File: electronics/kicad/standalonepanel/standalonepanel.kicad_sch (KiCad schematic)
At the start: 84 parts, among them J1 Speaker, J2 POWER, P1 USB-C, P2 USB-A, SW1 TST-ESP32, SW2 BOOT, SW3 TST-ICE40, SW4 RESET, U1 SC189ZSKTRT, U10 MPU-6050, U2 SC189ZSKTRT, U3 ESP32-WROVER-E, U4 CH340C, U5 MAX3421E, U6 IS64WV25616EFBLL-10TLI, U7 ICE40-HX4K, U8 DS3231M, U9 MAX98357A, X2 12MHz

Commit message: fix schematic errors: - swapped TxD/RxD + resistor CH340 - corrected footprint of DS3231 (was too big) textual errors of U2 (C-variant 1.2V)
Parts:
- D2: value 1N5819WS -> BAT760
- R2: value 33R -> 47R
- U2: value SC189ZSKTRT -> SC189CSKTRT
- U8: value DS3231M -> DS3231; footprint Package_SO:SO-16_3.9x9.9mm_P1.27mm -> Package_SO:SOIC-16W_7.5x10.3mm_P1.27mm
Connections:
- net at U3.34 (U0RXD/GPIO3): now also R2.1; no longer U4.3 (RXD)
- net at U3.35 (U0TXD/GPIO1): now also U4.3 (RXD); no longer R2.1
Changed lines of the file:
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@@
 	(wire
 		(pts
-			(xy 318.77 33.02) (xy 396.24 33.02)
+			(xy 318.77 33.02) (xy 374.65 33.02)
 		)
 		(stroke
@@
 	(wire
 		(pts
-			(xy 393.7 30.48) (xy 393.7 63.5)
-		)
-		(stroke
-			(width 0)
-			(type default)
-		)
-	)
-	(wire
-		(pts
 			(xy 269.24 173.99) (xy 278.13 173.99)
 		)
@@
 	(wire
 		(pts
-			(xy 383.54 30.48) (xy 393.7 30.48)
-		)
-		(stroke
-			(width 0)
-			(type default)
-		)
-	)
-	(wire
-		(pts
 			(xy 60.96 142.24) (xy 62.23 142.24)
 		)
@@
 	(wire
 		(pts
+			(xy 398.78 66.04) (xy 398.78 30.48)
+		)
+		(stroke
+			(width 0)
+			(type default)
+		)
+	)
+	(wire
+		(pts
 			(xy 318.77 55.88) (xy 320.04 55.88)
 		)
@@
 	(wire
 		(pts
-			(xy 318.77 30.48) (xy 375.92 30.48)
-		)
-		(stroke
-			(width 0)
-			(type default)
-		)
-	)
-	(wire
-		(pts
-			(xy 388.62 66.04) (xy 396.24 66.04)
+			(xy 318.77 30.48) (xy 398.78 30.48)
 		)
 		(stroke
@@
 	(wire
 		(pts
-			(xy 396.24 33.02) (xy 396.24 66.04)
-		)
-		(stroke
-			(width 0)
-			(type default)
-		)
-	)
-	(wire
-		(pts
 			(xy 60.96 106.68) (xy 62.23 106.68)
 		)
@@
 	(wire
 		(pts
+			(xy 388.62 66.04) (xy 398.78 66.04)
+		)
+		(stroke
+			(width 0)
+			(type default)
+		)
+	)
+	(wire
+		(pts
 			(xy 372.11 170.18) (xy 375.92 170.18)
 		)
@@
 	(wire
 		(pts
-			(xy 80.01 154.94) (xy 80.01 158.75)
+			(xy 396.24 33.02) (xy 396.24 63.5)
 		)
 		(stroke
@@
 	(wire
 		(pts
-			(xy 74.93 44.45) (xy 74.93 45.72)
+			(xy 80.01 154.94) (xy 80.01 158.75)
 		)
 		(stroke
@@
 	(wire
 		(pts
-			(xy 137.16 71.12) (xy 137.16 72.39)
+			(xy 74.93 44.45) (xy 74.93 45.72)
 		)
 		(stroke
@@
 	(wire
 		(pts
-			(xy 317.5 127) (xy 322.58 127)
+			(xy 137.16 71.12) (xy 137.16 72.39)
 		)
 		(stroke
@@
 	(wire
 		(pts
-			(xy 149.86 45.72) (xy 170.18 45.72)
+			(xy 317.5 127) (xy 322.58 127)
 		)
 		(stroke
@@
 	(wire
 		(pts
-			(xy 167.64 195.58) (xy 167.64 209.55)
+			(xy 149.86 45.72) (xy 170.18 45.72)
 		)
 		(stroke
@@
 	(wire
 		(pts
-			(xy 262.89 162.56) (xy 262.89 163.83)
+			(xy 167.64 195.58) (xy 167.64 209.55)
 		)
 		(stroke
@@
 	(wire
 		(pts
-			(xy 388.62 63.5) (xy 393.7 63.5)
+			(xy 262.89 162.56) (xy 262.89 163.83)
 		)
 		(stroke
@@
 	(wire
 		(pts
+			(xy 382.27 33.02) (xy 396.24 33.02)
+		)
+		(stroke
+			(width 0)
+			(type default)
+		)
+	)
+	(wire
+		(pts
 			(xy 88.9 30.48) (xy 93.98 30.48)
 		)
@@
 	(wire
 		(pts
+			(xy 396.24 63.5) (xy 388.62 63.5)
+		)
+		(stroke
+			(width 0)
+			(type default)
+		)
+	)
+	(wire
+		(pts
 			(xy 88.9 26.67) (xy 88.9 27.94)
 		)
@@
 			)
 		)
-		(property "Value" "1N5819WS"
+		(property "Value" "BAT760"
 			(at 234.95 90.17 0)
 			(effects
@@
 			)
 		)
-		(property "Value" "DS3231M"
-			(at 303.022 232.918 0)
+		(property "Value" "DS3231"
+			(at 300.736 231.648 0)
 			(effects
 				(font
@@
 			)
 		)
-		(property "Footprint" "Package_SO:SO-16_3.9x9.9mm_P1.27mm"
+		(property "Footprint" "Package_SO:SOIC-16W_7.5x10.3mm_P1.27mm"
 			(at 297.18 237.49 0)
 			(effects
@@
 	)
 	(symbol
-		(lib_id "Device:R")
-		(at 379.73 30.48 90)
-		(unit 1)
-		(exclude_from_sim no)
-		(in_bom yes)
-		(on_board yes)
-		(dnp no)
-		(property "Reference" "R2"
-			(at 384.1962 29.1831 90)
-			(effects
-				(font
-					(size 1 1)
-				)
-			)
-		)
-		(property "Value" "33R"
-			(at 379.73 30.48 90)
-			(effects
-				(font
-					(size 1 1)
-				)
-			)
-		)
-		(property "Footprint" "Resistor_SMD:R_1206_3216Metric_Pad1.30x1.75mm_HandSolder"
-			(at 379.73 32.258 90)
-			(effects
-				(font
-					(size 1.27 1.27)
-				)
-				(hide yes)
-			)
-		)
-		(property "Datasheet" "~"
-			(at 379.73 30.48 0)
-			(effects
-				(font
-					(size 1.27 1.27)
-				)
-				(hide yes)
-			)
-		)
-		(property "Description" "Resistor"
-			(at 379.73 30.48 0)
-			(effects
-				(font
-					(size 1.27 1.27)
-				)
-				(hide yes)
-			)
-		)
-		(pin "1"
-		)
-		(pin "2"
-		)
-		(instances
-			(project "standalonepanel"
-				(path "/982fd936-c5cb-43af-8607-60f832a26f93"
-					(reference "R2")
-					(unit 1)
-				)
-			)
-		)
-	)
-	(symbol
 		(lib_id "power:+3V3")
 		(at 53.34 60.96 0)
@@
 	)
 	(symbol
+		(lib_id "Device:R")
+		(at 378.46 33.02 90)
+		(unit 1)
+		(exclude_from_sim no)
+		(in_bom yes)
+		(on_board yes)
+		(dnp no)
+		(property "Reference" "R2"
+			(at 382.9262 31.7231 90)
+			(effects
+				(font
+					(size 1 1)
+				)
+			)
+		)
+		(property "Value" "47R"
+			(at 378.46 33.02 90)
+			(effects
+				(font
+					(size 1 1)
+				)
+			)
+		)
+		(property "Footprint" "Resistor_SMD:R_1206_3216Metric_Pad1.30x1.75mm_HandSolder"
+			(at 378.46 34.798 90)
+			(effects
+				(font
+					(size 1.27 1.27)
+				)
+				(hide yes)
+			)
+		)
+		(property "Datasheet" "~"
+			(at 378.46 33.02 0)
+			(effects
+				(font
+					(size 1.27 1.27)
+				)
+				(hide yes)
+			)
+		)
+		(property "Description" "Resistor"
+			(at 378.46 33.02 0)
+			(effects
+				(font
+					(size 1.27 1.27)
+				)
+				(hide yes)
+			)
+		)
+		(pin "1"
+		)
+		(pin "2"
+		)
+		(instances
+			(project "standalonepanel"
+				(path "/982fd936-c5cb-43af-8607-60f832a26f93"
+					(reference "R2")
+					(unit 1)
+				)
+			)
+		)
+	)
+	(symbol
 		(lib_id "0_project:C")
 		(at 154.94 223.52 270)
@@
 			)
 		)
-		(property "Value" "SC189ZSKTRT"
+		(property "Value" "SC189CSKTRT"
 			(at 104.14 36.83 0)
 			(effects

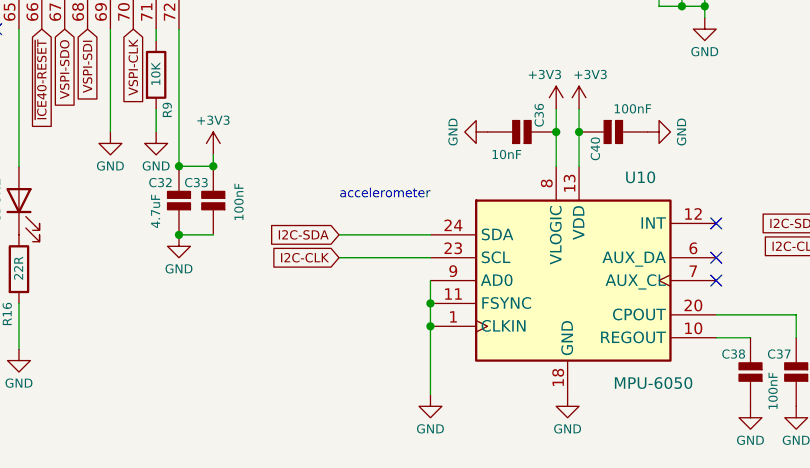
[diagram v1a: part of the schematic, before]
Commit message: changed I2C address of MPU6050 from 0x68 to 0x69 to remove conflict with DS3231
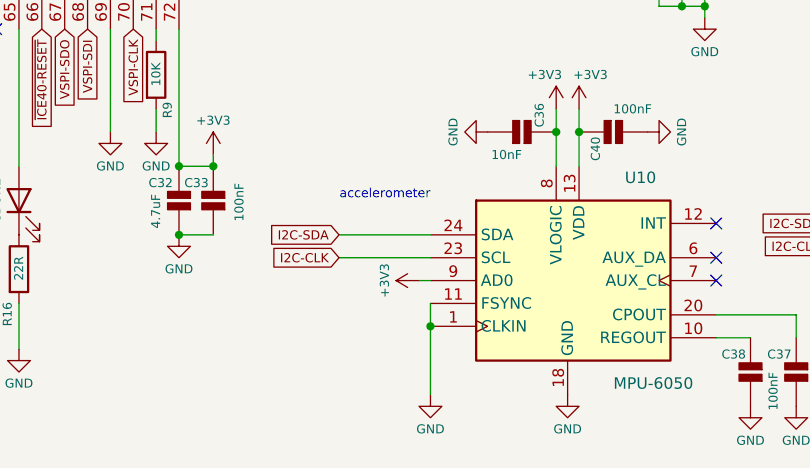
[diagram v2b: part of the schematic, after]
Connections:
- net +3V3: now also U10.9 (AD0)
- net GND: no longer U10.9 (AD0)
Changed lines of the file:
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@@
 	)
 	(junction
-		(at 233.68 226.06)
-		(diameter 0)
-		(color 0 0 0 0)
-	)
-	(junction
 		(at 17.78 43.18)
 		(diameter 0)
@@
 	(wire
 		(pts
+			(xy 232.41 223.52) (xy 233.68 223.52)
+		)
+		(stroke
+			(width 0)
+			(type default)
+		)
+	)
+	(wire
+		(pts
 			(xy 242.57 120.65) (xy 247.65 120.65)
 		)
@@
 	(wire
 		(pts
-			(xy 233.68 223.52) (xy 233.68 226.06)
-		)
-		(stroke
-			(width 0)
-			(type default)
-		)
-	)
-	(wire
-		(pts
 			(xy 306.07 186.69) (xy 306.07 190.5)
 		)
@@
 					(unit 1)
 				)
+			)
+		)
+	)
+	(symbol
+		(lib_id "power:+3V3")
+		(at 232.41 223.52 90)
+		(unit 1)
+		(exclude_from_sim no)
+		(in_bom yes)
+		(on_board yes)
+		(dnp no)
+		(property "Reference" "#PWR092"
+			(at 236.22 223.52 0)
+			(effects
+				(font
+					(size 1.27 1.27)
+				)
+				(hide yes)
+			)
+		)
+		(property "Value" "+3V3"
+			(at 228.6 223.52 0)
+			(effects
+				(font
+					(size 1 1)
+				)
+			)
+		)
+		(property "Footprint" ""
+			(at 232.41 223.52 0)
+			(effects
+				(font
+					(size 1.27 1.27)
+				)
+				(hide yes)
+			)
+		)
+		(property "Datasheet" ""
+			(at 232.41 223.52 0)
+			(effects
+				(font
+					(size 1.27 1.27)
+				)
+				(hide yes)
+			)
+		)
+		(property "Description" "Power symbol creates a global label with name \"+3V3\""
+			(at 232.41 223.52 0)
+			(effects
+				(font
+					(size 1.27 1.27)
+				)
+				(hide yes)
+			)
+		)
+		(pin "1"
+		)
+		(instances
+			(project "standalonepanel"
+				(path "/982fd936-c5cb-43af-8607-60f832a26f93"
+					(reference "#PWR092")
+					(unit 1)
+				)

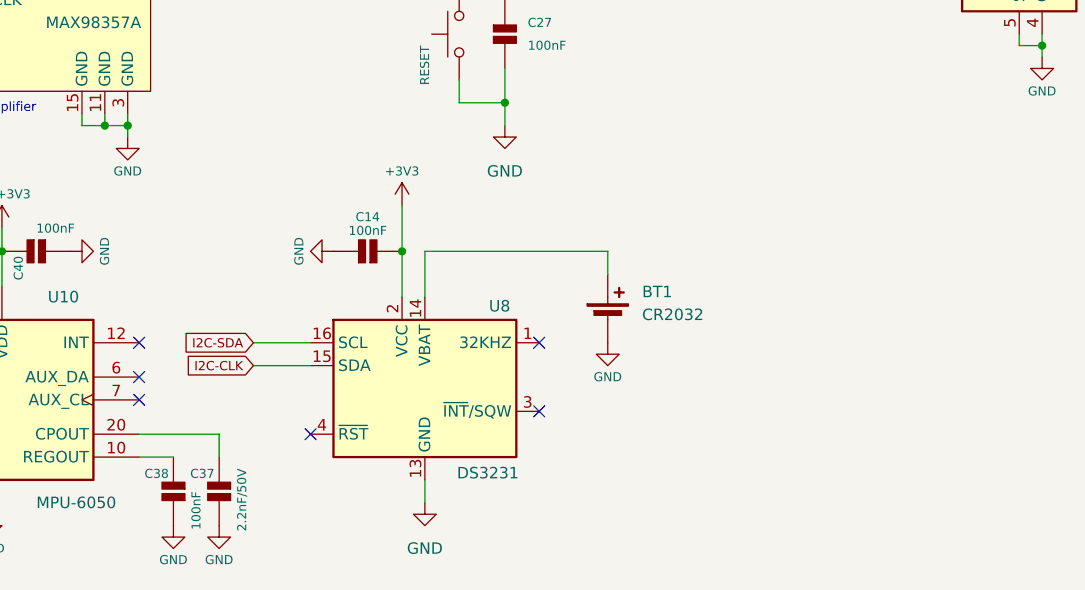
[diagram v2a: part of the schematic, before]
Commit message: added SDA and SCL pullup resistors swapped teh SDA and SCL lines for DS3231
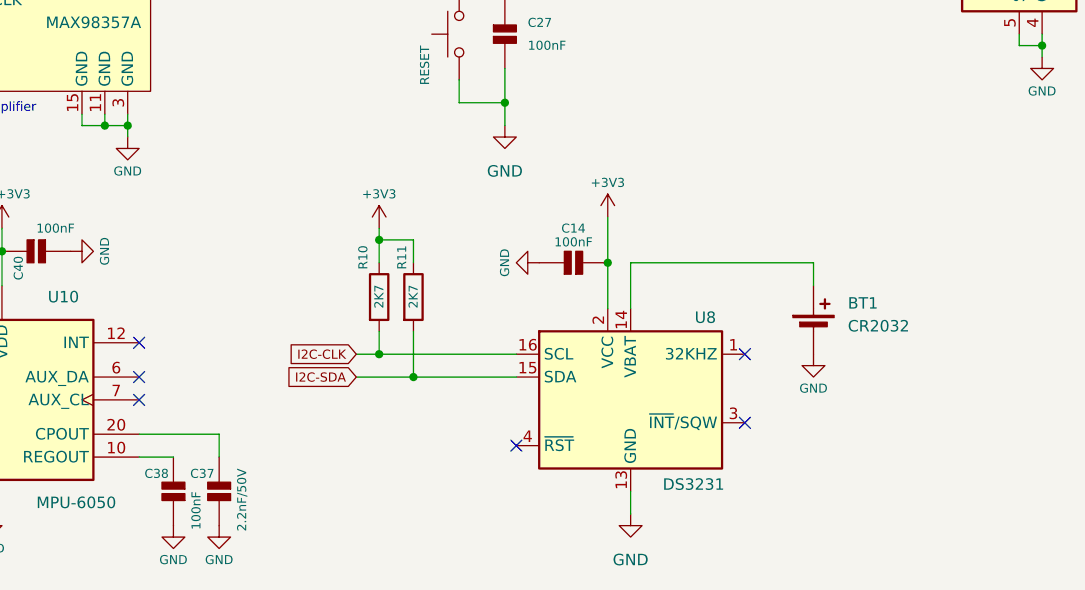
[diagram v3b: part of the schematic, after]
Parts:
- added R10, R11: 2K7, Resistor_SMD:R_1206_3216Metric_Pad1.30x1.75mm_HandSolder, symbol Device:R
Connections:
- net +3V3: now also R10.1, R11.1
- net I2C-CLK: now also U8.16 (SCL), R10.2; no longer U8.15 (SDA)
- net I2C-SDA: now also U8.15 (SDA), R11.2; no longer U8.16 (SCL)
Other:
- moved on the sheet: BT1, C14, U8

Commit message: added clamps for attaching panel to wooden frame (this clamps turned out a little too high though)
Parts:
- removed F1: 500mA, 0_project:FUSEHOLDER 1808, symbol 0_project:Fuse
- removed P1: USB-C, 0_project:USB_C_Receptacle_G-Switch_GT-USB-7010ASV, symbol 0_project:USB_C
- removed P2: USB-A, 0_project:USB-A TH Female, symbol 0_project:USB_A
- removed U5: MAX3421E, 0_project:PQFP-32_5x5mm_P0.5mm, symbol 0_project:MAX3421E
- added C39, C41, C42, C43, C44: 1uF, Capacitor_SMD:C_0805_2012Metric_Pad1.18x1.45mm_HandSolder, symbol 0_project:C
- added D1: BAT760, Diode_SMD:D_SOD-323, symbol Diode:1N5819WS
- added D3, D4: P4SMA27A, symbol 0_project:PTVS5V0Z1USK
- added J3: USB_C_Receptacle, symbol Connector:USB_C_Receptacle
- added Q1: AO4435, Package_SO:SOIC-8_3.9x4.9mm_P1.27mm, symbol 0_project:AO4435
- added R18: 100R, Resistor_SMD:R_1206_3216Metric_Pad1.30x1.75mm_HandSolder, symbol Device:R
- added R19, R21: 22K, Resistor_SMD:R_1206_3216Metric_Pad1.30x1.75mm_HandSolder, symbol Device:R
- added R20, R22: 100K, Resistor_SMD:R_1206_3216Metric_Pad1.30x1.75mm_HandSolder, symbol Device:R
- added SW5: BUTTON2, Button_Switch_SMD:SW_SPST_FSMSM, symbol Switch:SW_Push
- added SW6: BUTTON3, Button_Switch_SMD:SW_SPST_FSMSM, symbol Switch:SW_Push
- added U11: 74LVC1G00, 0_project:SOT23-5-SC189_SEM, symbol 74xGxx:74LVC1G00
- added U5: STUSB4500QTR, Package_DFN_QFN:QFN-24-1EP_4x4mm_P0.5mm_EP2.7x2.7mm, symbol Interface_USB:STUSB4500QTR
- C17: value 1uF -> 100nF
- R12: value 33R -> 100R
- R13: value 33R -> 100K
- R14: value 100R -> 10K
- R6: value 5K1 -> 10K
- SW1: value TST-ESP32 -> BUTTON1
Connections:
- net +3V3: now also R14.1, R6.1, U10.3 (NC), U11.5 (VCC); no longer C17.2, R6.2
- net GND: now also C17.2, LED1.1 (K), C39.2, C41.2, C42.2, C43.2, C44.2, D3.2 (A), D4.2 (A), J3.A1 (GND), J3.A12 (GND), J3.B1 (GND), J3.B12 (GND), J3.S1 (SHIELD), SW5.1, SW6.1, U11.3 (GND), U5.10 (GND), U5.12 (ADDR0), U5.13 (ADDR1), U5.22 (VSYS), U5.25 (GND); no longer C17.1, C27.2, R5.2
- net I2C-CLK: now also U5.7 (SCL)
- net I2C-SDA: now also U5.8 (SDA)
- net ~{RESET}: now also R12.1, U11.2; no longer R14.1
- net at U3.35 (U0TXD/GPIO1): no longer U4.3 (RXD)
- net at U3.6 (GPIO34/ADC1_CH6): now also R14.2, SW5.2
- net at U3.7 (GPIO35/ADC1_CH7): now also R15.2, SW6.2
- net at U3.9 (32K_XN/GPIO33/ADC1_CH5): now also R5.1; no longer LED1.2 (A)
- net VBUS: now reaches R13.1
- net VBUS: now also C3.1, C5.1, U1.1 (VIN), U1.3 (EN), U2.1 (VIN), U2.3 (EN), C42.1, C44.1, D1.2 (A), D4.1 (K), J3.A4 (VBUS), J3.A9 (VBUS), J3.B4 (VBUS), J3.B9 (VBUS), Q1.1 (S1), R20.1, U5.24 (VDD)
- net at U4.5 (UD+): now also J3.A6 (D+), J3.B6 (D+)
- net at U4.6 (UD-): now also J3.A7 (D-), J3.B7 (D-)
- net at R12.2: now also C17.1, R6.2, SW4.2
- net at R13.2: now also Q1.4 (G1), R18.2, R19.1
- removed net +5V: C3.1, C5.1, J2.1 (Pin_1), U1.1 (VIN), U1.3 (EN), U2.1 (VIN), U2.3 (EN)
- new net: C27.2, R18.1
- new net: LED1.2 (A), R5.2
- new net: J3.A5 (CC1), U5.1 (CC1DB), U5.2 (CC1)
- new net: R19.2, U5.16 (VBUS_EN_SNK)
- new net: R21.2, U5.18 (VBUS_VS_DISCH)
- new net: C41.1, U5.21 (VREG_1V2)
- new net: C39.1, U5.23 (VREG_2V7)
- new net: J3.B5 (CC2), U5.4 (CC2), U5.5 (CC2DB)
- new net: R22.2, U5.9 (DISCH)
- new net: C43.1, D1.1 (K), R20.2, R21.1
- new net RESET: U11.4, U5.6 (RESET)
- new net VPanel: C27.1, D3.1 (K), J2.1 (Pin_1), Q1.5 (D1), R22.1
- no-connect marks 79 -> 74
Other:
- note added: "USB PD Sink I2C:0x28"
- note added: "accelerometer I2C:0x69"
- note added: "realtime clock I2C:0x68"
- note removed: "USB Host for keyboard"
- note removed: "accelerometer"
- moved on the sheet: C23, C24, C36, C37, C38, C40, HUB75E-1, HUB75E-2, J1, R2, SW2, U10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

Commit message: Schematic v2 PCB version v2 send for production
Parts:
- removed C20: 100nF, Capacitor_SMD:C_0805_2012Metric_Pad1.18x1.45mm_HandSolder, symbol 0_project:C
- removed C23: 10uF, Capacitor_SMD:C_0805_2012Metric_Pad1.18x1.45mm_HandSolder, symbol 0_project:C
- removed D3, D4: P4SMA27A, symbol 0_project:PTVS5V0Z1USK
- removed J1: Speaker, Connector_JST:JST_XH_S2B-XH-A_1x02_P2.50mm_Horizontal, symbol Connector_Generic:Conn_01x02
- removed J2: POWER, Connector_JST:JST_XH_S2B-XH-A_1x02_P2.50mm_Horizontal, symbol Connector_Generic:Conn_01x02
- removed J3: USB_C_Receptacle, symbol Connector:USB_C_Receptacle
- removed R14, R15: 10K, Resistor_SMD:R_1206_3216Metric_Pad1.30x1.75mm_HandSolder, symbol Device:R
- removed SW5: BUTTON2, Button_Switch_SMD:SW_SPST_FSMSM, symbol Switch:SW_Push
- removed SW6: BUTTON3, Button_Switch_SMD:SW_SPST_FSMSM, symbol Switch:SW_Push
- removed U11: 74LVC1G00, 0_project:SOT23-5-SC189_SEM, symbol 74xGxx:74LVC1G00
- removed U5: STUSB4500QTR, Package_DFN_QFN:QFN-24-1EP_4x4mm_P0.5mm_EP2.7x2.7mm, symbol Interface_USB:STUSB4500QTR
- removed U6: IS64WV25616EFBLL-10TLI, Package_SO:TSOP-II-44_10.16x18.41mm_P0.8mm, symbol 0_project:IS64WV25616EFBLL
- removed U9: MAX98357A, Package_DFN_QFN:TQFN-16-1EP_3x3mm_P0.5mm_EP1.6x1.6mm, symbol 0_project:MAX98357A
- added C25, C29: 100nF, Capacitor_SMD:C_0805_2012Metric_Pad1.18x1.45mm_HandSolder, symbol 0_project:C
- added C28: 10uF, Capacitor_SMD:C_0805_2012Metric_Pad1.18x1.45mm_HandSolder, symbol 0_project:C
- added D1, D4, D5, D6: P4SMA27A, Diode_SMD:D_SMA_Handsoldering, symbol 0_project:P4SMA27A
- added J1: LEDPWR, 0_project:JST_VH_1x04_P3.96mm_Horizontal, symbol Connector_Generic:Conn_01x04
- added J2: USB_C-PD, 0_project:USB_C_Receptacle_G-Switch_GT-USB-7010ASV, symbol 0_project:USB_C-PD
- added J3: Speaker, Connector_JST:JST_XH_S2B-XH-A_1x02_P2.50mm_Horizontal, symbol Connector_Generic:Conn_01x02
- added LED4: PD, LED_SMD:LED_1206_3216Metric_Pad1.42x1.75mm_HandSolder, symbol Device:LED
- added R16: 1K5, Resistor_SMD:R_1206_3216Metric_Pad1.30x1.75mm_HandSolder, symbol Device:R
- added R17, R6, R7: 10K, Resistor_SMD:R_1206_3216Metric_Pad1.30x1.75mm_HandSolder, symbol Device:R
- added SW3: UP, 0_project:SW_Tactile_SKHH_Angled, symbol Switch:SW_Push
- added SW4: DOWN, 0_project:SW_Tactile_SKHH_Angled, symbol Switch:SW_Push
- added U5: IS64WV25616EFBLL-10TLI, Package_SO:TSOP-II-44_10.16x18.41mm_P0.8mm, symbol 0_project:IS64WV25616EFBLL
- added U6: STUSB4500QTR, 0_project:QFN-24-1EP_4x4mm_P0.5mm_EP2.7x2.7mm, symbol 0_project:STUSB4500QTR
- added U8: MAX98357A, Package_DFN_QFN:TQFN-16-1EP_3x3mm_P0.5mm_EP1.6x1.6mm, symbol 0_project:MAX98357A
- R11: renamed from R22; value 100K -> 1K
- R13: renamed from R20; value 100K -> 470R
- R15: renamed from R21; value 22K -> 1K
- SW1: value BUTTON1 -> SET; footprint Button_Switch_SMD:SW_SPST_FSMSM -> 0_project:SW_Tactile_SKHH_Angled; PCBTXT (none) -> SET
- renumbered C13 to C12, C12 to C13, C27 to C14, C44 to C15, C43 to C16, C15 to C17, C16 to C18, C39 to C19, C41 to C20, C42 to C21, C18 to C22, C19 to C23, C21 to C26, C22 to C27, C25 to C30, C26 to C31, C36 to C32, C40 to C33, C30 to C34, C31 to C35, C32 to C36, C33 to C37, C28 to C38, C29 to C39, C34 to C40, C35 to C41, C38 to C42, C37 to C43, C14 to C44, C17 to C45, D1 to D3, LED2 to LED1, LED1 to LED2, LED4 to LED5, R3 to R1, R13 to R10, R18 to R12, R19 to R14, R9 to R18, R16 to R19, R1 to R2, R17 to R20, R6 to R21, R12 to R22, R10 to R23, R11 to R24, R2 to R3, R7 to R8, R8 to R9, SW3 to SW5, SW4 to SW6, U8 to U10, U4 to U3, U3 to U4, U10 to U9, X2 to X1
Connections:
- net +3V3: now also C25.1, C28.1, C29.1, R16.2, R6.1, R7.1, U5.11 (VDD), U5.33 (VDD), U8.7 (VDD), U8.8 (VDD); no longer U9.3 (NC)
- net GND: now also C28.2, C29.2, D1.2 (A), D4.2 (A), D5.2 (A), D6.2 (A), J1.3 (Pin_3), J1.4 (Pin_4), J2.A1 (GND), J2.A12 (GND), J2.B1 (GND), J2.B12 (GND), J2.S1 (SHIELD), R17.2, SW3.1, SW4.1, U5.12 (GND), U5.34 (GND), U5.39 (~{LB}), U5.40 (~{UB}), U6.10 (GND), U6.12 (ADDR0), U6.13 (ADDR1), U6.22 (VSYS), U6.25 (GND), U8.11 (GND), U8.15 (GND), U8.2 (GAIN_SLOT), U8.3 (GND)
- net I2C-CLK: now also U6.7 (SCL)
- net I2C-SDA: now also U6.8 (SDA)
- net RAM-A0: now also U5.1 (A0)
- net RAM-A1: now also U5.2 (A1)
- net RAM-A10: now also U5.23 (A10)
- net RAM-A11: now also U5.24 (A11)
- net RAM-A12: now also U5.25 (A12)
- net RAM-A13: now also U5.26 (A13)
- net RAM-A14: now also U5.27 (A14)
- net RAM-A15: now also U5.42 (A15)
- net RAM-A16: now also U5.43 (A16)
- net RAM-A17: now also U5.44 (A17)
- net RAM-A2: now also U5.3 (A2)
- net RAM-A3: now also U5.4 (A3)
- net RAM-A4: now also U5.5 (A4)
- net RAM-A5: now also U5.18 (A5)
- net RAM-A6: now also U5.19 (A6)
- net RAM-A7: now also U5.20 (A7)
- net RAM-A8: now also U5.21 (A8)
- net RAM-A9: now also U5.22 (A9)
- net RAM-CS: now also U5.6 (~{CE})
- net RAM-D0: now also U5.7 (D0)
- net RAM-D1: now also U5.8 (D1)
- net RAM-D10: now also U5.31 (D10)
- net RAM-D11: now also U5.32 (D11)
- net RAM-D12: now also U5.35 (D12)
- net RAM-D13: now also U5.36 (D13)
- net RAM-D14: now also U5.37 (D14)
- net RAM-D15: now also U5.38 (D15)
- net RAM-D2: now also U5.9 (D2)
- net RAM-D3: now also U5.10 (D3)
- net RAM-D4: now also U5.13 (D4)
- net RAM-D5: now also U5.14 (D5)
- net RAM-D6: now also U5.15 (D6)
- net RAM-D7: now also U5.16 (D7)
- net RAM-D8: now also U5.29 (D8)
- net RAM-D9: now also U5.30 (D9)
- net RAM-OE: now also U5.41 (~{OE})
- net RAM-WE: now also U5.17 (~{WE})
- net VBUS: now also Q1.2 (S1), Q1.3 (S1), D4.1 (K), J2.A4 (VBUS), J2.A9 (VBUS), J2.B4 (VBUS), J2.B9 (VBUS), U6.24 (VDD)
- net at U4.35 (U0TXD/GPIO1): now also U3.3 (RXD)
- net at U4.6 (GPIO34/ADC1_CH6): now also R7.2, SW4.2
- net at U4.7 (GPIO35/ADC1_CH7): now also R6.2, SW3.2
- net at R14.2: now also U6.16 (VBUS_EN_SNK)
- net at R15.2: now also U6.18 (VBUS_VS_DISCH)
- net at C20.1: now also U6.21 (VREG_1V2)
- net at C19.1: now also U6.23 (VREG_2V7)
- net at R11.2: now also U6.9 (DISCH)
- net at U3.5 (UD+): now also J2.A6 (D+), J2.B6 (D+)
- net at U3.6 (UD-): now also J2.A7 (D-), J2.B7 (D-)
- net at U7.15 (IOL_10A): now also U8.4 (~{SD_MODE})
- net at U7.16 (IOL_10B): now also U8.1 (DIN)
- net at U7.17 (IOL_12A): now also U8.16 (BCLK)
- net at U7.18 (IOL_12B): now also U8.14 (LRCLK)
- net HSPI-CLK: no longer names the net of U4.13 (MTMS/GPIO14/ADC2_CH6)
- net HSPI-CS-USB: no longer names the net of U4.12 (ADC2_CH7/GPIO27)
- net HSPI-INT: no longer names the net of U4.23 (MTDO/GPIO15/ADC2_CH3)
- net HSPI-SDI: no longer names the net of U4.16 (MTCK/GPIO13/ADC2_CH4)
- net HSPI-SDO: no longer names the net of U4.14 (MTDI/GPIO12/ADC2_CH5)
- net VPanel renamed VPANEL
- net VPANEL: now also Q1.6 (D1), Q1.7 (D1), Q1.8 (D1), D1.1 (K), J1.1 (Pin_1), J1.2 (Pin_2)
- new net: D6.1 (K), J2.B5 (CC2), U6.4 (CC2), U6.5 (CC2DB)
- new net: D5.1 (K), J2.A5 (CC1), U6.1 (CC1DB), U6.2 (CC1)
- new net: LED4.1 (K), U6.19 (ALERT)
- new net: C25.2, R17.1, U6.6 (RESET)
- new net: J3.1 (Pin_1), U8.9 (OUTP)
- new net: J3.2 (Pin_2), U8.10 (OUTN)
- new net: LED4.2 (A), R16.1
- no-connect marks 74 -> 78
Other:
- moved on the sheet: C45, R21, R22
